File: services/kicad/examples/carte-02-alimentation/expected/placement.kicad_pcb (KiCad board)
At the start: 2 copper layers, 34.8 x 25.3 mm, 12 parts, among them J1 IN_5V, J2 OUT, U1 AMS1117-3.3, U2 AMS1117-1.8

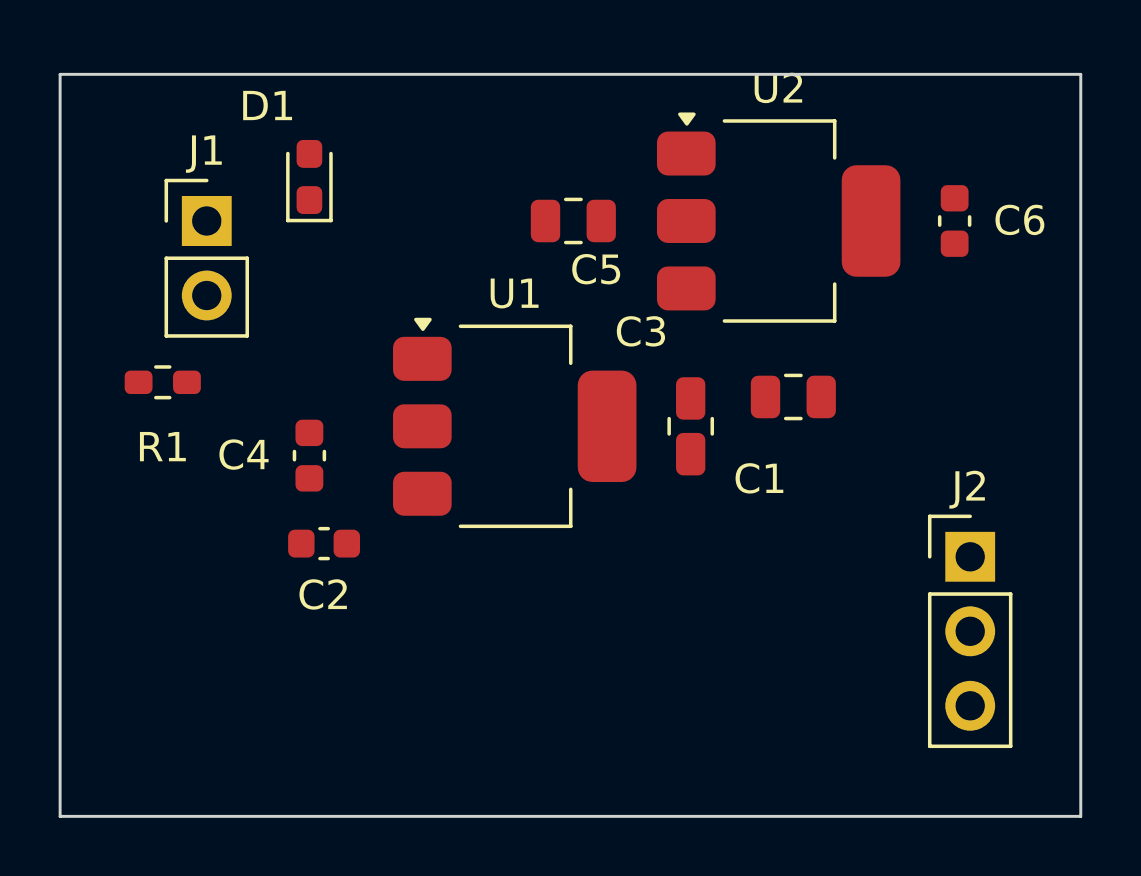
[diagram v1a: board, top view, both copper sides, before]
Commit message: fix(kicad): plan de masse referme — banc DIX cartes sur dix, 0 erreur 0 manquante (#237)
* docs(kicad): la derniere rupture de plan tient a UN segment, pas a un faisceau

Diagnostic complet du seul defaut restant du banc (carte-10), mesure sur le
board qui le porte vraiment, apres consultation de Codex et de GLM.

Mesures sur `/tmp/livr/carte-10-maximale/route.kicad_pcb` (33 violations,
0 erreur, 1 connexion manquante) :

- 23 ilots GND sur les deux faces, exactement 2 orphelins, et ce sont des
  JUMEAUX : F.Cu 1,30 mm2 (porte la pastille C35.2) et B.Cu 0,99 mm2.
- AUCUN de leurs points n a le plan principal en vis-a-vis : ils se font face
  l un l autre. La piste « changer de face par un via », proposee par GLM, est
  donc REFUTEE par la mesure.
- La couture de production visite les deux ilots et refuse la totalite de
  leurs sites (23 et 18 candidats ; obstacle 16/10, hors_polygone 6/7,
  trou_trop_pres 1/1) : un via ne tient pas dans un millimetre carre.
  Le raccord par courte piste rend relies 0, sans_chemin 19.
- Mais le plan principal n est qu a 0,862 mm sur F.Cu et 0,781 mm sur B.Cu, et
  UN SEUL segment coupe le couloir de chaque face (EXT2_1, EXT4_1).

Le plan de Codex — deplacer l obstacle au lieu de chercher un passage a
travers — a donc ici un ensemble a arracher d UN segment par face, pas une
recherche ouverte. Decision de strategie de routage : D-2026-09-22-a, EN
ATTENTE. Rien n est implemente.

Levier natif verifie et jamais appele : LocalRerouter.reroute_segment() de
kicad-tools, utilise par drc/repair_clearance.py, zero appelant Cirqix. Il
travaille sur le document S-expression quand notre code travaille sur pcbnew.

Lecons inscrites dans CLAUDE.md :
- j ai d abord mesure le board VERSIONNE du 21, qui est propre (non_connectes
  0) et se pretait a toutes les demonstrations — un via y tenait avec 0,29 mm
  de marge. Verifier que l artefact PORTE le defaut avant de le diagnostiquer.
- ma premiere sonde raisonnait zone par zone, alors que la carte por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
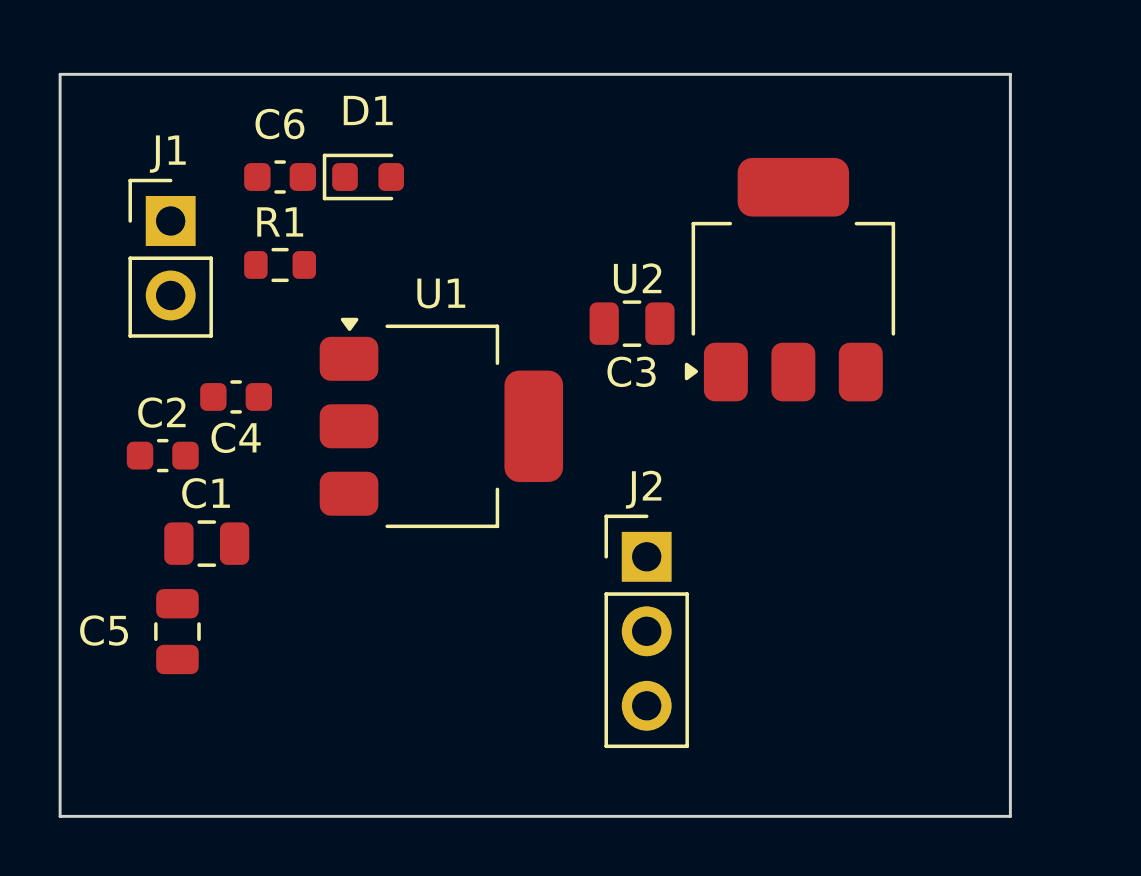
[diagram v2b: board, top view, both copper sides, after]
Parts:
- moved C6 23.0 mm to (128.5, 88.5), turned to 180 degrees
- moved C1 20.6 mm to (126.0, 101.0), turned to 0 degrees
- moved C5 19.4 mm to (125.0, 104.0), turned to 90 degrees
- moved J2 11.0 mm to (141.0, 101.5)
- moved C2 6.26 mm to (124.5, 98.0)
- moved R1 5.66 mm to (128.5, 91.5), turned to 0 degrees
- moved C3 4.03 mm to (140.5, 93.5), turned to 180 degrees
- moved C4 3.20 mm to (127.0, 96.0), turned to 180 degrees
- moved U1 2.50 mm to (134.0, 97.0)
- moved U2 2.06 mm to (146.0, 92.0), turned to 90 degrees
- moved D1 2.00 mm to (131.5, 88.5), turned to 0 degrees
- moved J1 1.23 mm to (124.8, 90.0)
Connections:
- U1 pad 3: VIN -> PWR_FLAG
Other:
- board size 34.8 x 25.3 mm -> 32.4 x 25.3 mm
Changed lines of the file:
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@@
 (kicad_pcb
-	(version 20260206)
+	(version 20241229)
 	(generator "kicad_tools")
 	(generator_version "10.0")
@@
 	(title_block
 		(title "Cirqix PCB")
-		(date "2026-09-12")
+		(date "2026-09-23")
 		(rev 1.0)
 		(company "")
@@
 	(net 4 "VIN")
 	(net 5 "LED_A")
+	(net 6 "PWR_FLAG")
 	(footprint "PinHeader_1x02_P2.54mm_Vertical"
 		(version 20260206)
 		(generator "kicad-footprint-generator")
 		(layer "F.Cu")
-		(at 126 90 0)
+		(at 124.77 90)
 		(descr "Through hole straight pin header, 1x02, 2.54mm pitch, single row")
 		(tags "Through hole pin header THT 1x02 2.54mm single row")
@@
 		(generator_version "10.0")
 		(layer "F.Cu")
-		(at 136.5 97 0)
+		(at 134 97)
 		(descr "module CMS SOT223 4 pins")
 		(tags "CMS SOT")
@@
 			(layers "F.Cu" "F.Mask" "F.Paste")
 			(roundrect_rratio 0.25)
-			(net 4 "VIN")
+			(net 6 "PWR_FLAG")
 		)
 		(embedded_fonts no)
@@
 		(generator_version "10.0")
 		(layer "F.Cu")
-		(at 145.5 90 0)
+		(at 146 92 90)
 		(descr "module CMS SOT223 4 pins")
 		(tags "CMS SOT")
 		(property "Reference" "U2"
-			(at 0 -4.5 0)
+			(at -1.46958e-16 -5.3 0)
 			(layer "F.SilkS")
 			(effects
@@
 		)
 		(pad "1" smd roundrect
-			(at -3.15 -2.3)
+			(at -3.15 -2.3 90)
 			(size 2 1.5)
 			(layers "F.Cu" "F.Mask" "F.Paste")
@@
 		)
 		(pad "2" smd roundrect
-			(at -3.15 0)
+			(at -3.15 0 90)
 			(size 2 1.5)
 			(layers "F.Cu" "F.Mask" "F.Paste")
@@
 		)
 		(pad "2" smd roundrect
-			(at 3.15 0)
+			(at 3.15 0 90)
 			(size 2 3.8)
 			(layers "F.Cu" "F.Mask" "F.Paste")
@@
 		)
 		(pad "3" smd roundrect
-			(at -3.15 2.3)
+			(at -3.15 2.3 90)
 			(size 2 1.5)
 			(layers "F.Cu" "F.Mask" "F.Paste")
@@
 		(generator "kicad-footprint-generator")
 		(layer "F.Cu")
-		(at 146 96 180)
+		(at 126 101)
 		(descr "Capacitor SMD 0805 (2012 Metric), square (rectangular) end terminal, IPC-7351 nominal, (Body size source: IPC-SM-782 page 76, https://www.pcb-3d.com/wordpress/wp-content/uploads/ipc-sm-782a_amendment_1_and_2.pdf, https://docs.google.com/spreadsheets/d/1BsfQQcO9C6DZCsRaXUlFlo91Tg2WpOkGARC1WS5S8t0/edit?usp=sharing)")
 		(tags "capacitor")
 		(property "Reference" "C1"
-			(at 1.13137 -2.81137 0)
+			(at 0 -1.68 0)
 			(layer "F.SilkS")
 			(effects
@@
 		)
 		(pad "1" smd roundrect
-			(at -0.95 0 180)
+			(at -0.95 0)
 			(size 1 1.45)
 			(layers "F.Cu" "F.Mask" "F.Paste")
@@
 		)
 		(pad "2" smd roundrect
-			(at 0.95 0 180)
+			(at 0.95 0)
 			(size 1 1.45)
 			(layers "F.Cu" "F.Mask" "F.Paste")
@@
 		(generator "kicad-footprint-generator")
 		(layer "F.Cu")
-		(at 130 101 0)
+		(at 124.5 98)
 		(descr "Capacitor SMD 0603 (1608 Metric), square (rectangular) end terminal, IPC-7351 nominal, (Body size source: IPC-SM-782 page 76, https://www.pcb-3d.com/wordpress/wp-content/uploads/ipc-sm-782a_amendment_1_and_2.pdf)")
 		(tags "capacitor")
 		(property "Reference" "C2"
-			(at 1.95943e-16 1.77 0)
+			(at 0 -1.43 0)
 			(layer "F.SilkS")
 			(effects
@@
 		(generator "kicad-footprint-generator")
 		(layer "F.Cu")
-		(at 142.5 97 90)
+		(at 140.5 93.5 180)
 		(descr "Capacitor SMD 0805 (2012 Metric), square (rectangular) end terminal, IPC-7351 nominal, (Body size source: IPC-SM-782 page 76, https://www.pcb-3d.com/wordpress/wp-content/uploads/ipc-sm-782a_amendment_1_and_2.pdf, https://docs.google.com/spreadsheets/d/1BsfQQcO9C6DZCsRaXUlFlo91Tg2WpOkGARC1WS5S8t0/edit?usp=sharing)")
 		(tags "capacitor")
 		(property "Reference" "C3"
-			(at 3.2 -1.68 0)
+			(at 0 -1.68 0)
 			(layer "F.SilkS")
 			(effects
@@
 		)
 		(pad "1" smd roundrect
-			(at -0.95 0)
+			(at -0.95 0 180)
 			(size 1 1.45)
 			(layers "F.Cu" "F.Mask" "F.Paste")
@@
 		)
 		(pad "2" smd roundrect
-			(at 0.95 0)
+			(at 0.95 0 180)
 			(size 1 1.45)
 			(layers "F.Cu" "F.Mask" "F.Paste")
@@
 		(generator "kicad-footprint-generator")
 		(layer "F.Cu")
-		(at 129.5 98 90)
+		(at 127 96 180)
 		(descr "Capacitor SMD 0603 (1608 Metric), square (rectangular) end terminal, IPC-7351 nominal, (Body size source: IPC-SM-782 page 76, https://www.pcb-3d.com/wordpress/wp-content/uploads/ipc-sm-782a_amendment_1_and_2.pdf)")
 		(tags "capacitor")
 		(property "Reference" "C4"
-			(at -1.46958e-16 -2.23 0)
+			(at 0 -1.43 0)
 			(layer "F.SilkS")
 			(effects
@@
 		)
 		(pad "1" smd roundrect
-			(at -0.775 0 90)
+			(at -0.775 0 180)
 			(size 0.9 0.95)
 			(layers "F.Cu" "F.Mask" "F.Paste")
@@
 		)
 		(pad "2" smd roundrect
-			(at 0.775 0 90)
+			(at 0.775 0 180)
 			(size 0.9 0.95)
 			(layers "F.Cu" "F.Mask" "F.Paste")
@@
 		(generator "kicad-footprint-generator")
 		(layer "F.Cu")
-		(at 138.5 90 180)
+		(at 125 104 90)
 		(descr "Capacitor SMD 0805 (2012 Metric), square (rectangular) end terminal, IPC-7351 nominal, (Body size source: IPC-SM-782 page 76, https://www.pcb-3d.com/wordpress/wp-content/uploads/ipc-sm-782a_amendment_1_and_2.pdf, https://docs.google.com/spreadsheets/d/1BsfQQcO9C6DZCsRaXUlFlo91Tg2WpOkGARC1WS5S8t0/edit?usp=sharing)")
 		(tags "capacitor")
 		(property "Reference" "C5"
-			(at -0.8 -1.68 0)
+			(at -1.46958e-16 -2.48 0)
 			(layer "F.SilkS")
 			(effects
@@
 		)
 		(pad "1" smd roundrect
-			(at -0.95 0 180)
+			(at -0.95 0 90)
 			(size 1 1.45)
 			(layers "F.Cu" "F.Mask" "F.Paste")
@@
 		)
 		(pad "2" smd roundrect
-			(at 0.95 0 180)
+			(at 0.95 0 90)
 			(size 1 1.45)
 			(layers "F.Cu" "F.Mask" "F.Paste")
@@
 		(generator "kicad-footprint-generator")
 		(layer "F.Cu")
-		(at 151.5 90 270)
+		(at 128.5 88.5 180)
 		(descr "Capacitor SMD 0603 (1608 Metric), square (rectangular) end terminal, IPC-7351 nominal, (Body size source: IPC-SM-782 page 76, https://www.pcb-3d.com/wordpress/wp-content/uploads/ipc-sm-782a_amendment_1_and_2.pdf)")
 		(tags "capacitor")
 		(property "Reference" "C6"
-			(at -1.46958e-16 -2.23 0)
+			(at 1.95943e-16 1.77 0)
 			(layer "F.SilkS")
 			(effects
@@
 		)
 		(pad "1" smd roundrect
-			(at -0.775 0 270)
+			(at -0.775 0 180)
 			(size 0.9 0.95)
 			(layers "F.Cu" "F.Mask" "F.Paste")
@@
 		)
 		(pad "2" smd roundrect
-			(at 0.775 0 270)
+			(at 0.775 0 180)
 			(size 0.9 0.95)
 			(layers "F.Cu" "F.Mask" "F.Paste")
@@
 		(generator "kicad-footprint-generator")
 		(layer "F.Cu")
-		(at 124.5 95.5 180)
+		(at 128.5 91.5)
 		(descr "Resistor SMD 0603 (1608 Metric), square (rectangular) end terminal, IPC-7351 nominal, (Body size source: IPC-SM-782 page 72, https://www.pcb-3d.com/wordpress/wp-content/uploads/ipc-sm-782a_amendment_1_and_2.pdf)")
 		(tags "resistor")
 		(property "Reference" "R1"
-			(at -1.46958e-16 -2.23 0)
+			(at 0 -1.43 0)
 			(layer "F.SilkS")
 			(effects
@@
 		)
 		(pad "1" smd roundrect
-			(at -0.825 0 270)
+			(at -0.825 0)
 			(size 0.8 0.95)
 			(layers "F.Cu" "F.Mask" "F.Paste")
@@
 		)
 		(pad "2" smd roundrect
-			(at 0.825 0 270)
+			(at 0.825 0)
 			(size 0.8 0.95)
 			(layers "F.Cu" "F.Mask" "F.Paste")
@@
 		(generator "kicad-footprint-generator")
 		(layer "F.Cu")
-		(at 129.5 88.5 90)
+		(at 131.5 88.5)
 		(descr "LED SMD 0603 (1608 Metric), square (rectangular) end terminal, IPC-7351 nominal, (Body size source: http://www.tortai-tech.com/upload/download/2011102023233369053.pdf)")
 		(tags "LED")
 		(property "Reference" "D1"
-			(at 2.4 -1.43 0)
+			(at -1.46958e-16 -2.23 0)
 			(layer "F.SilkS")
 			(effects
@@
 		)
 		(pad "1" smd roundrect
-			(at -0.7875 0 180)
+			(at -0.7875 0)
 			(size 0.875 0.95)
 			(layers "F.Cu" "F.Mask" "F.Paste")
@@
 		)
 		(pad "2" smd roundrect
-			(at 0.7875 0 180)
+			(at 0.7875 0)
 			(size 0.875 0.95)
 			(layers "F.Cu" "F.Mask" "F.Paste")
@@
 		(generator "kicad-footprint-generator")
 		(layer "F.Cu")
-		(at 152.03 101.45 0)
+		(at 141 101.45)
 		(descr "Through hole straight pin header, 1x03, 2.54mm pitch, single row")
 		(tags "Through hole pin header THT 1x03 2.54mm single row")
@@
 	)
 	(gr_rect
-		(start 121.0 85.0)
-		(end 155.8 110.3)
+		(start 121.000 85.000)
+		(end 153.400 110.300)
 		(stroke
 			(width 0.1)
